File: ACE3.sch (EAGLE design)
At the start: 141 parts, among them IC1 7805T, IC2 74HCT04N, IC4 74LS32N, Q1 2N3904, Q3 BC237, T1 2N2369, X1 6.556MHz

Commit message: Sent test of ACE2NOKB for PCB manufacture as risk reduction execise to show schematic works.
Signed-off-by: John Bradley <flypie@rocketmail.com>
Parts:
- removed POWER-9V-DC-IN: 1503_04, con-lumberg:1503_04
- removed VIDEO-OUT: WBTOR1, con-lumberg:WBTOR1
- added COMPOSITE-OUT, POWER-IN-9V-DC: (no value), con-amp-mt:L02P
- AUDIO-IN, AUDIO-OUT: value 1503_04 -> (none); device con-lumberg:1503_04 -> con-amp-mt:L02P
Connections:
- new net N$83: IC2F.I, Z26C.O
- net /RD: now also Z24B.I1; no longer Z26C.I1
- net /WR: now also Z24A.I1; no longer Z25C.I1
- net ADDRESS11: now also Z25C.I1; no longer Z24B.I1
- net CSB4KV: now also IC2F.O; no longer Z24A.O
- net CST4KV: now also Z25C.O, Z26C.I1; no longer Z24A.I1, Z24B.O
- net GND: now also AUDIO-IN-2.S, AUDIO-OUT-2.S, COMPOSITE-OUT-2.S, POWER-IN-9V-DC-2.S; no longer AUDIO-IN.2, AUDIO-OUT.2, POWER-9V-DC-IN.2, VIDEO-OUT.S
- net N$12: now also AUDIO-IN-1.S; no longer AUDIO-IN.1, AUDIO-IN.3
- net N$29: now also IC2C.O; no longer IC2C.I, Z26C.O
- net N$31: now also Z24A.I0, Z24B.I0; no longer Z25C.I0, Z26C.I0
- net N$35: now also Z24A.O; no longer Z25C.O
- net N$39: now also IC2C.I, Z24B.O; no longer IC2C.O
- net N$43: now also AUDIO-OUT-1.S; no longer AUDIO-OUT.1, AUDIO-OUT.3
- net N$65: now also POWER-IN-9V-DC-1.S; no longer POWER-9V-DC-IN.1, POWER-9V-DC-IN.3
- net N$86: now also Z25C.I0, Z26C.I0; no longer Z24A.I0, Z24B.I0
- net VIDEO: now also COMPOSITE-OUT-1.S; no longer VIDEO-OUT.T
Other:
- moved on the sheet: IC2C, IC2F, IC4C, Z24A, Z24B, Z25C, Z26C

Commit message: tidy
Signed-off-by: John Bradley <flypie@rocketmail.com>
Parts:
- removed Z52: CY62256, memory-idt:71256P
- D1, D10, D11, D2, D3, D4, D5, D6, D7, D8, D9: value 1N4148DO35-7 -> 1N4148DO35; device diode:1N4148DO35-7 -> diode:DIODE-D-2.5
- Z1-2: value 2764 -> (none); device memory:2764 -> memory:27256
- Z3-4: value CY62256 -> AS6C1008-55PCN; device memory-idt:71256P -> AS6C1008-55PCN:AS6C1008-55PCN
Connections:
- removed net CY1: Z22C.O, Z52G$1.!CS
- removed net CY62256: Z3-4G$1.!CS, Z50A.O
- new net N$72: Z50A.O, Z50B.I0
- new net N$87: Z19D.I0, Z19D.I1, Z3-4.CE, Z50B.O
- new net N$88: Z19D.O, Z3-4.CE2
- net /RD: now also Z3-4.OE; no longer Z3-4G$1.!OE, Z52G$1.!OE
- net /WR: now also Z3-4.WE; no longer Z3-4G$1.!WE, Z52G$1.!WE
- net ADDRESS0: now also Z3-4.A0; no longer Z3-4G$1.A0, Z52G$1.A0
- net ADDRESS1: now also Z3-4.A1; no longer Z3-4G$1.A1, Z52G$1.A1
- net ADDRESS10: now also Z3-4.A10; no longer Z3-4G$1.A10, Z52G$1.A10
- net ADDRESS11: now also Z3-4.A11; no longer Z3-4G$1.A11, Z52G$1.A11
- net ADDRESS12: now also Z3-4.A12; no longer Z3-4G$1.A12, Z52G$1.A12
- net ADDRESS13: now also Z1-2A.A13, Z3-4.A13; no longer Z3-4G$1.A13, Z52G$1.A13
- net ADDRESS14: now also Z1-2A.A14, Z3-4.A14; no longer Z3-4G$1.A14, Z52G$1.A14
- net ADDRESS15: now also Z3-4.A15
- net ADDRESS2: now also Z3-4.A2; no longer Z3-4G$1.A2, Z52G$1.A2
- net ADDRESS3: now also Z3-4.A3; no longer Z3-4G$1.A3, Z52G$1.A3
- net ADDRESS4: now also Z3-4.A4; no longer Z3-4G$1.A4, Z52G$1.A4
- net ADDRESS5: now also Z3-4.A5; no longer Z3-4G$1.A5, Z52G$1.A5
- net ADDRESS6: now also Z3-4.A6; no longer Z3-4G$1.A6, Z52G$1.A6
- net ADDRESS7: now also Z3-4.A7; no longer Z3-4G$1.A7, Z52G$1.A7
- net ADDRESS8: now also Z3-4.A8; no longer Z3-4G$1.A8, Z52G$1.A8
- net ADDRESS9: now also Z3-4.A9; no longer Z3-4G$1.A9, Z52G$1.A9
- net DATA0: now also Z3-4.DQ0; no longer Z3-4G$1.I/O1, Z52G$1.I/O1
- net DATA1: now also Z3-4.DQ1; no longer Z3-4G$1.I/O2, Z52G$1.I/O2
- net DATA2: now also Z3-4.DQ2; no longer Z3-4G$1.I/O3, Z52G$1.I/O3
- net DATA3: now also Z3-4.DQ3; no longer Z3-4G$1.I/O4, Z52G$1.I/O4
- net DATA4: now also Z3-4.DQ4; no longer Z3-4G$1.I/O5, Z52G$1.I/O5
- net DATA5: now also Z3-4.DQ5; no longer Z3-4G$1.I/O6, Z52G$1.I/O6
- net DATA6: now also Z3-4.DQ6; no longer Z3-4G$1.I/O7, Z52G$1.I/O7
- net DATA7: now also Z3-4.DQ7; no longer Z3-4G$1.I/O8, Z52G$1.I/O8
- net GND: now also Z3-4.A16
- net N$23: now also Z50B.I1; no longer Z22C.I0
- net N$25: now also Z50B.I2; no longer Z22C.I1
- net N$28: now also Z50B.I3; no longer Z22C.I2
- net VCC: no longer Z1-2A.!PGM, Z1-2A.VPP
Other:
- moved on the sheet: Z19D, Z50A, Z50B

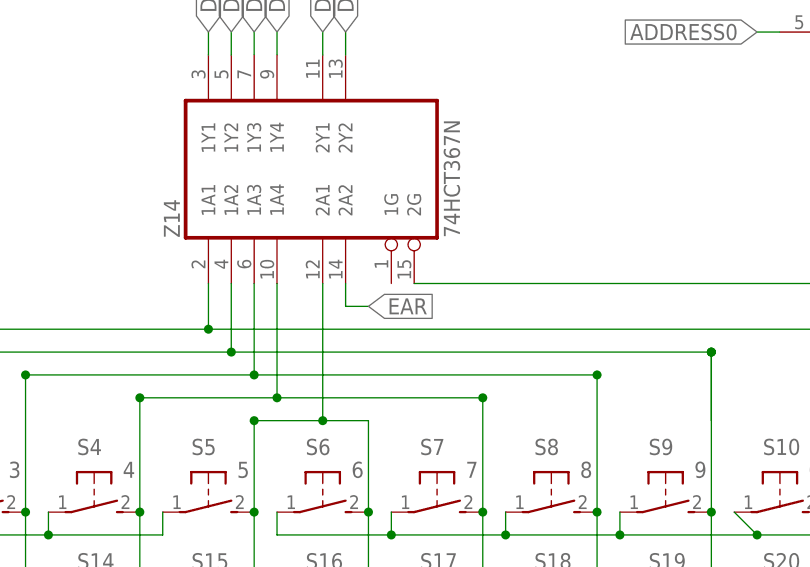
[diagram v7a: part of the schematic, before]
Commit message: Change to KiCad up date to latest board thinking include boards with Z84C15 and revised memeory architecture, last 8K paged and IO mapp tidied. Extra sysmbols for KiCad are in the library.zip add them to the global Libraries.
Signed-off-by: John Bradley <flypie@rocketmail.com>
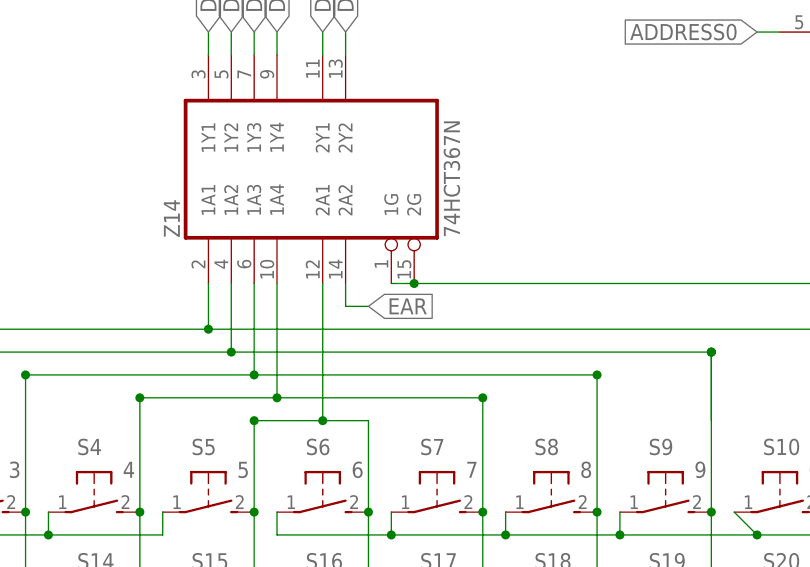
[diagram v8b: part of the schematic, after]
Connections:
- net N$29: now also Z14A.1G
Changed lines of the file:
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@@
 <?xml version="1.0" encoding="utf-8"?>
 <!DOCTYPE eagle SYSTEM "eagle.dtd">
-<eagle version="9.4.1">
+<eagle version="9.4.2">
 <drawing>
 <settings>
@@
 <wire x1="55.88" y1="-248.92" x2="55.88" y2="-243.84" width="0.1524" layer="91"/>
 <wire x1="55.88" y1="-243.84" x2="53.34" y2="-243.84" width="0.1524" layer="91"/>
+<pinref part="Z14" gate="A" pin="1G"/>
+<wire x1="-40.64" y1="-243.84" x2="-38.1" y2="-243.84" width="0.1524" layer="91"/>
+<junction x="-38.1" y="-243.84"/>
 </segment>
 </net>
